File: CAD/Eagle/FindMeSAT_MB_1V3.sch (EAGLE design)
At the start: 137 parts, among them Q101 ABS07-32.768KHZ, Q651 ABM3B-16MHZ-10-R50-1-U, U1001 CFPT-141-20MHZ, U101 ATXMEGA256A3BU-AU, U1011 OPA354, U1021 OPA354, U1111 LM2831YMF, U1121 LM4120IM5-3.0, U201 SIM808, U301 MPU-9250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

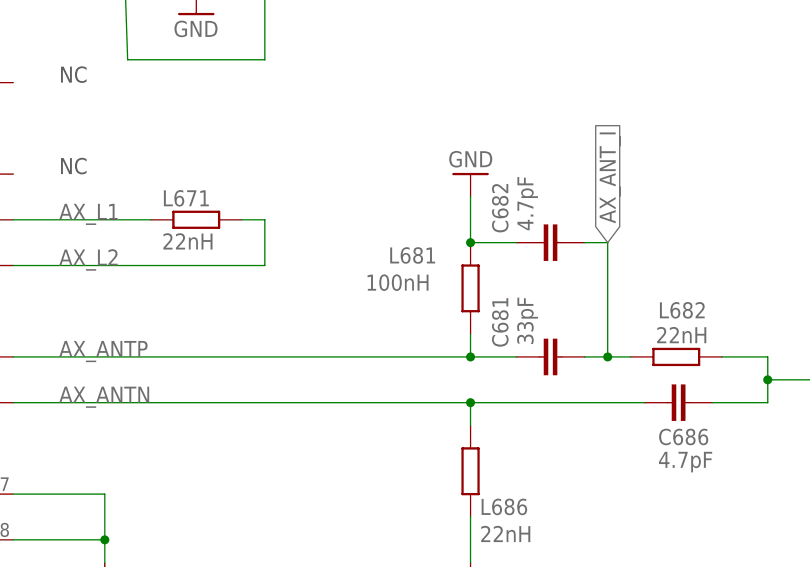
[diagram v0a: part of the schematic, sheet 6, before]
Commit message: HW_V1.3 - one inductivity reversed to 150nH
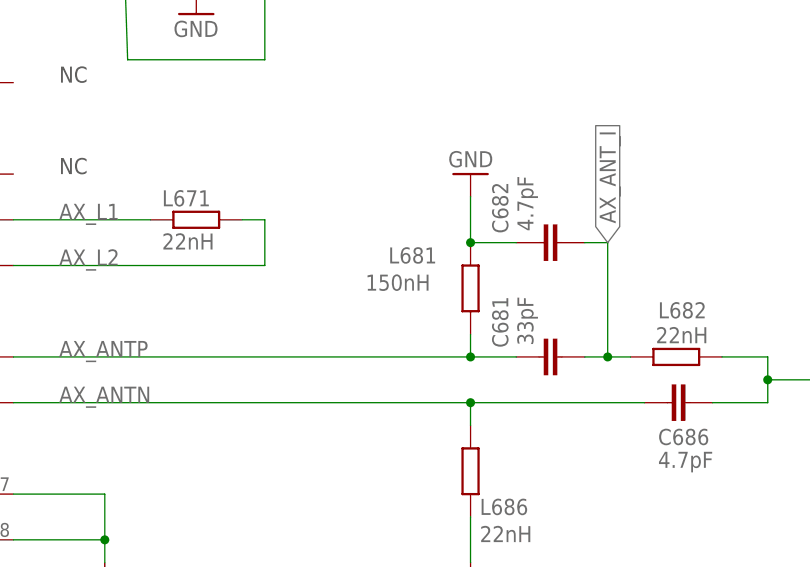
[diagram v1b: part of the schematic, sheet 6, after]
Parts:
- L681: value 100nH -> 150nH
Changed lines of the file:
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@@
 <part name="GND684" library="df4iah_supply" deviceset="GND" device=""/>
 <part name="C686" library="rcl" deviceset="C-EU" device="C0603" value="4.7pF"/>
-<part name="L681" library="rcl" deviceset="R-EU_" device="R0603" value="100nH"/>
+<part name="L681" library="rcl" deviceset="R-EU_" device="R0603" value="150nH"/>
 <part name="X685" library="df4iah_connector" deviceset="SMA_SMT_AMPHENOL-901-143" device="" value="SMA_CON"/>
 <part name="GND689" library="df4iah_supply" deviceset="GND" device=""/>

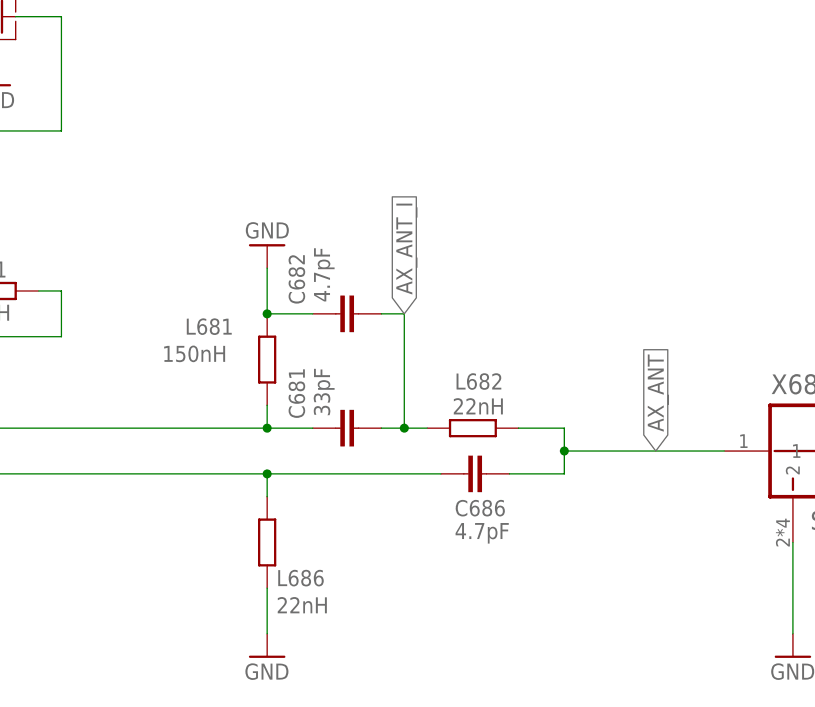
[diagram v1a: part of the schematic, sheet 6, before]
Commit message: HW_V1.3 - L687 added, AX5243 UHF matching unit enhanced
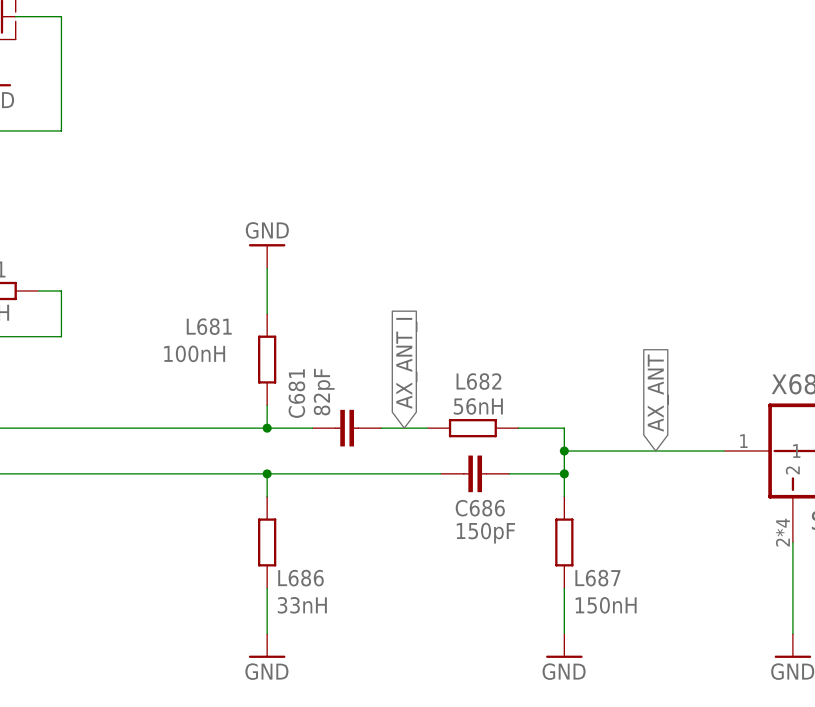
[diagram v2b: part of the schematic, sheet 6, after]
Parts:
- removed C682: 4.7pF, rcl:C-EUC0603
- added L687: 150nH, rcl:R-EU_R0603
- C681: value 33pF -> 82pF
- C686: value 4.7pF -> 150pF
- L681: value 150nH -> 100nH
- L682: value 22nH -> 56nH
- L686: value 22nH -> 33nH
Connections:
- net AX_ANT: now also L687.2
- net AX_ANT_I: no longer C682.2
- net GND: now also L687.1; no longer C682.1
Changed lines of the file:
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@@
 <part name="Q651" library="df4iah_crystal" deviceset="ABM03B-16.000MHZ" device="" value="ABM3B-16MHZ-10-R50-1-U"/>
 <part name="L671" library="rcl" deviceset="R-EU_" device="R0603" value="22nH"/>
-<part name="C681" library="rcl" deviceset="C-EU" device="C0603" value="33pF"/>
+<part name="C681" library="rcl" deviceset="C-EU" device="C0603" value="82pF"/>
 <part name="GND683" library="df4iah_supply" deviceset="GND" device=""/>
-<part name="L686" library="rcl" deviceset="R-EU_" device="R0603" value="22nH"/>
-<part name="L682" library="rcl" deviceset="R-EU_" device="R0603" value="22nH"/>
+<part name="L686" library="rcl" deviceset="R-EU_" device="R0603" value="33nH"/>
+<part name="L682" library="rcl" deviceset="R-EU_" device="R0603" value="56nH"/>
 <part name="GND684" library="df4iah_supply" deviceset="GND" device=""/>
-<part name="C686" library="rcl" deviceset="C-EU" device="C0603" value="4.7pF"/>
-<part name="L681" library="rcl" deviceset="R-EU_" device="R0603" value="150nH"/>
+<part name="C686" library="rcl" deviceset="C-EU" device="C0603" value="150pF"/>
+<part name="L681" library="rcl" deviceset="R-EU_" device="R0603" value="100nH"/>
 <part name="X685" library="df4iah_connector" deviceset="SMA_SMT_AMPHENOL-901-143" device="" value="SMA_CON"/>
 <part name="GND689" library="df4iah_supply" deviceset="GND" device=""/>
@@
 <part name="C1141" library="rcl" deviceset="C-EU" device="C0603" value="100pF"/>
 <part name="C302" library="rcl" deviceset="C-EU" device="C0603" value="10nF"/>
-<part name="C682" library="rcl" deviceset="C-EU" device="C0603" value="4.7pF"/>
+<part name="L687" library="rcl" deviceset="R-EU_" device="R0603" value="150nH"/>
+<part name="GND1" library="df4iah_supply" deviceset="GND" device=""/>
 </parts>
 <sheets>
@@
 <instance part="GND689" gate="1" x="226.06" y="63.5"/>
 <instance part="GND651" gate="1" x="137.16" y="127"/>
-<instance part="C682" gate="G$1" x="175.26" y="101.6" smashed="yes" rot="R90">
-<attribute name="NAME" x="171.831" y="102.616" size="1.778" layer="95" rot="R90"/>
-<attribute name="VALUE" x="174.625" y="102.87" size="1.778" layer="96" rot="R90"/>
-</instance>
+<instance part="L687" gate="G$1" x="200.66" y="76.2" smashed="yes" rot="R90">
+<attribute name="NAME" x="201.676" y="71.3486" size="1.778" layer="95"/>
+<attribute name="VALUE" x="201.676" y="68.326" size="1.778" layer="96"/>
+</instance>
+<instance part="GND1" gate="1" x="200.66" y="63.5"/>
 </instances>
 <busses>
@@
 <pinref part="GND683" gate="1" pin="GND"/>
 <wire x1="167.64" y1="106.68" x2="167.64" y2="101.6" width="0.1524" layer="91"/>
-<pinref part="C682" gate="G$1" pin="1"/>
-<wire x1="167.64" y1="101.6" x2="172.72" y2="101.6" width="0.1524" layer="91"/>
-<junction x="167.64" y="101.6"/>
 </segment>
 <segment>
@@
 <pinref part="Q651" gate="G$1" pin="3"/>
 <pinref part="GND651" gate="1" pin="GND"/>
+</segment>
+<segment>
+<pinref part="GND1" gate="1" pin="GND"/>
+<pinref part="L687" gate="G$1" pin="1"/>
+<wire x1="200.66" y1="66.04" x2="200.66" y2="71.12" width="0.1524" layer="91"/>
 </segment>
 </net>
@@
 <wire x1="218.44" y1="86.36" x2="200.66" y2="86.36" width="0.1524" layer="91"/>
 <pinref part="X685" gate="A" pin="1"/>
+<pinref part="L687" gate="G$1" pin="2"/>
+<wire x1="200.66" y1="83.82" x2="200.66" y2="81.28" width="0.1524" layer="91"/>
+<junction x="200.66" y="83.82"/>
 </segment>
 </net>
@@
 <pinref part="C681" gate="G$1" pin="2"/>
 <pinref part="L682" gate="G$1" pin="1"/>
-<wire x1="180.34" y1="88.9" x2="182.88" y2="88.9" width="0.1524" layer="91"/>
-<pinref part="C682" gate="G$1" pin="2"/>
-<wire x1="182.88" y1="88.9" x2="185.42" y2="88.9" width="0.1524" layer="91"/>
-<wire x1="182.88" y1="88.9" x2="182.88" y2="101.6" width="0.1524" layer="91"/>
-<wire x1="182.88" y1="101.6" x2="180.34" y2="101.6" width="0.1524" layer="91"/>
-<junction x="182.88" y="88.9"/>
-<label x="182.88" y="101.6" size="1.778" layer="95" rot="R90" xref="yes"/>
+<wire x1="180.34" y1="88.9" x2="185.42" y2="88.9" width="0.1524" layer="91"/>
+<label x="182.88" y="88.9" size="1.778" layer="95" rot="R90" xref="yes"/>
 </segment>
 </net>
@@
 <segment>
 <pinref part="GND711" gate="1" pin="GND"/>
-<pinref part="C711" gate="G$1" pin="2"/>
 <wire x1="154.94" y1="127" x2="154.94" y2="129.54" width="0.1524" layer="91"/>
-<wire x1="154.94" y1="129.54" x2="142.24" y2="129.54" width="0.1524" layer="91"/>
-<wire x1="142.24" y1="129.54" x2="142.24" y2="132.08" width="0.1524" layer="91"/>
 <pinref part="C712" gate="G$1" pin="2"/>
 <wire x1="154.94" y1="129.54" x2="154.94" y2="132.08" width="0.1524" layer="91"/>
 <junction x="154.94" y="129.54"/>
-</segment>
-<segment>
+<wire x1="154.94" y1="129.54" x2="142.24" y2="129.54" width="0.1524" layer="91"/>
+<pinref part="C711" gate="G$1" pin="2"/>
+<wire x1="142.24" y1="129.54" x2="142.24" y2="132.08" width="0.1524" layer="91"/>
+</segment>
+<segment>

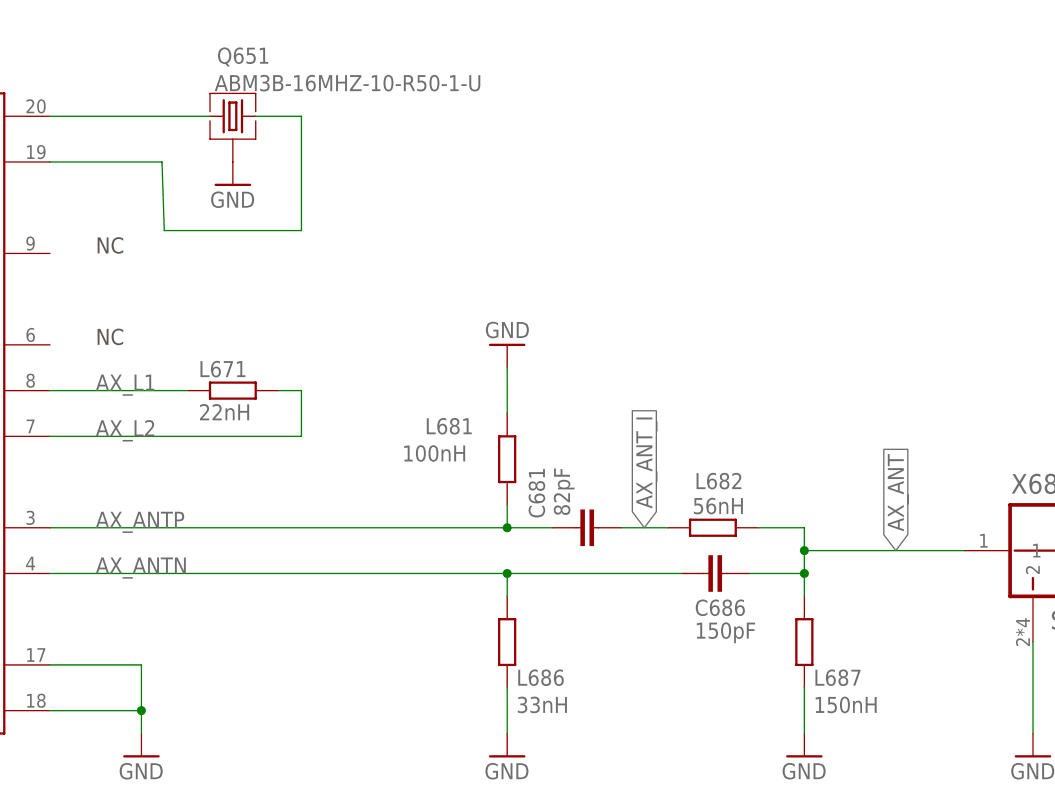
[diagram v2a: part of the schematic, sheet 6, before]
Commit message: HW_V1.3 - AX5243 - another matching setup
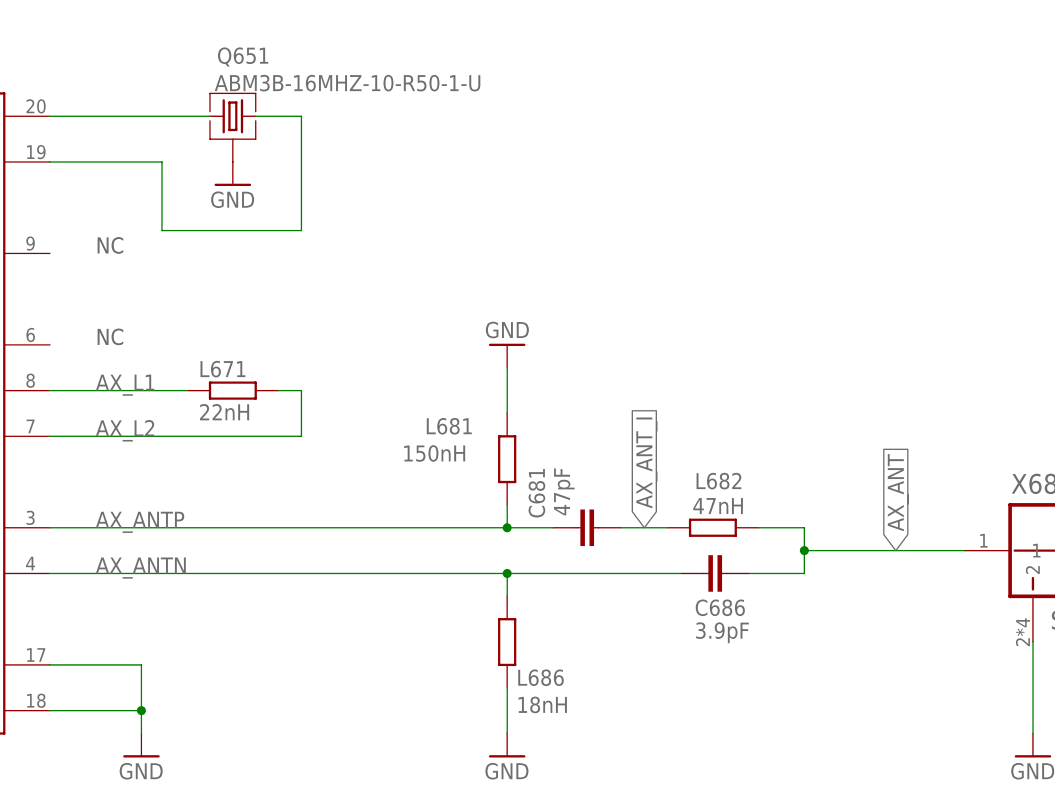
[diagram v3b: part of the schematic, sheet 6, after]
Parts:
- removed L687: 150nH, rcl:R-EU_R0603
- C681: value 82pF -> 47pF
- C686: value 150pF -> 3.9pF
- L681: value 100nH -> 150nH
- L682: value 56nH -> 47nH
- L686: value 33nH -> 18nH
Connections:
- net AX_ANT: no longer L687.2
- net GND: no longer L687.1
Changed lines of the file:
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@@
 <part name="Q651" library="df4iah_crystal" deviceset="ABM03B-16.000MHZ" device="" value="ABM3B-16MHZ-10-R50-1-U"/>
 <part name="L671" library="rcl" deviceset="R-EU_" device="R0603" value="22nH"/>
-<part name="C681" library="rcl" deviceset="C-EU" device="C0603" value="82pF"/>
+<part name="C681" library="rcl" deviceset="C-EU" device="C0603" value="47pF"/>
 <part name="GND683" library="df4iah_supply" deviceset="GND" device=""/>
-<part name="L686" library="rcl" deviceset="R-EU_" device="R0603" value="33nH"/>
-<part name="L682" library="rcl" deviceset="R-EU_" device="R0603" value="56nH"/>
+<part name="L686" library="rcl" deviceset="R-EU_" device="R0603" value="18nH"/>
+<part name="L682" library="rcl" deviceset="R-EU_" device="R0603" value="47nH"/>
 <part name="GND684" library="df4iah_supply" deviceset="GND" device=""/>
-<part name="C686" library="rcl" deviceset="C-EU" device="C0603" value="150pF"/>
-<part name="L681" library="rcl" deviceset="R-EU_" device="R0603" value="100nH"/>
+<part name="C686" library="rcl" deviceset="C-EU" device="C0603" value="3.9pF"/>
+<part name="L681" library="rcl" deviceset="R-EU_" device="R0603" value="150nH"/>
 <part name="X685" library="df4iah_connector" deviceset="SMA_SMT_AMPHENOL-901-143" device="" value="SMA_CON"/>
 <part name="GND689" library="df4iah_supply" deviceset="GND" device=""/>
@@
 <part name="C1141" library="rcl" deviceset="C-EU" device="C0603" value="100pF"/>
 <part name="C302" library="rcl" deviceset="C-EU" device="C0603" value="10nF"/>
-<part name="L687" library="rcl" deviceset="R-EU_" device="R0603" value="150nH"/>
-<part name="GND1" library="df4iah_supply" deviceset="GND" device=""/>
 </parts>
 <sheets>
@@
 <instance part="GND689" gate="1" x="226.06" y="63.5"/>
 <instance part="GND651" gate="1" x="137.16" y="127"/>
-<instance part="L687" gate="G$1" x="200.66" y="76.2" smashed="yes" rot="R90">
-<attribute name="NAME" x="201.676" y="71.3486" size="1.778" layer="95"/>
-<attribute name="VALUE" x="201.676" y="68.326" size="1.778" layer="96"/>
-</instance>
-<instance part="GND1" gate="1" x="200.66" y="63.5"/>
 </instances>
 <busses>
@@
 <pinref part="Q651" gate="G$1" pin="3"/>
 <pinref part="GND651" gate="1" pin="GND"/>
-</segment>
-<segment>
-<pinref part="GND1" gate="1" pin="GND"/>
-<pinref part="L687" gate="G$1" pin="1"/>
-<wire x1="200.66" y1="66.04" x2="200.66" y2="71.12" width="0.1524" layer="91"/>
 </segment>
 </net>
@@
 <wire x1="218.44" y1="86.36" x2="200.66" y2="86.36" width="0.1524" layer="91"/>
 <pinref part="X685" gate="A" pin="1"/>
-<pinref part="L687" gate="G$1" pin="2"/>
-<wire x1="200.66" y1="83.82" x2="200.66" y2="81.28" width="0.1524" layer="91"/>
-<junction x="200.66" y="83.82"/>
 </segment>
 </net>
@@
 <pinref part="U601" gate="A" pin="CLK16N"/>
 <wire x1="116.84" y1="129.54" x2="129.286" y2="129.54" width="0.1524" layer="91"/>
-<wire x1="129.286" y1="129.54" x2="129.54" y2="121.92" width="0.1524" layer="91"/>
-<wire x1="129.54" y1="121.92" x2="144.78" y2="121.92" width="0.1524" layer="91"/>
+<wire x1="129.286" y1="129.54" x2="129.286" y2="121.92" width="0.1524" layer="91"/>
+<wire x1="129.286" y1="121.92" x2="144.78" y2="121.92" width="0.1524" layer="91"/>
 <wire x1="144.78" y1="121.92" x2="144.78" y2="134.62" width="0.1524" layer="91"/>
 <pinref part="Q651" gate="G$1" pin="2"/>
